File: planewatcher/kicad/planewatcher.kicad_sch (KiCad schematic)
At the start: 7 parts, among them J1 Conn_01x02, J2 RF_IN, J3 FPGA BANK 33, J4 FPGA BANK 35 V1.2/V1.3, J5 BMI-S-209-F

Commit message: work on board layout
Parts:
- renumbered FL3 to FL2, J5 to J3, J3 to J4, J4 to J5
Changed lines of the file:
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@@
 		(dnp no)
 		(fields_autoplaced yes)
-		(property "Reference" "J4"
+		(property "Reference" "J5"
 			(at 105.41 137.16 0)
 			(show_name no)
@@
 			(project "planewatcher"
 				(path "/7a4a4324-e8b8-4d06-b75a-28095d4e9f10"
-					(reference "J4")
+					(reference "J5")
 					(unit 1)
 				)
@@
 		(in_pos_files yes)
 		(dnp no)
-		(property "Reference" "#PWR011"
+		(property "Reference" "#PWR03"
 			(at 146.05 45.72 0)
 			(hide yes)
@@
 			(project "planewatcher"
 				(path "/7a4a4324-e8b8-4d06-b75a-28095d4e9f10"
-					(reference "#PWR011")
+					(reference "#PWR03")
 					(unit 1)
 				)
@@
 		(in_pos_files yes)
 		(dnp no)
-		(property "Reference" "#PWR021"
+		(property "Reference" "#PWR04"
 			(at 185.42 48.26 0)
 			(hide yes)
@@
 			(project "planewatcher"
 				(path "/7a4a4324-e8b8-4d06-b75a-28095d4e9f10"
-					(reference "#PWR021")
+					(reference "#PWR04")
 					(unit 1)
 				)
@@
 		(in_pos_files yes)
 		(dnp no)
-		(property "Reference" "#PWR0146"
+		(property "Reference" "#PWR08"
 			(at 55.88 85.09 0)
 			(hide yes)
@@
 			(project "planewatcher"
 				(path "/7a4a4324-e8b8-4d06-b75a-28095d4e9f10"
-					(reference "#PWR0146")
+					(reference "#PWR08")
 					(unit 1)
 				)
@@
 		(in_pos_files yes)
 		(dnp no)
-		(property "Reference" "#PWR019"
+		(property "Reference" "#PWR013"
 			(at 100.33 111.76 0)
 			(hide yes)
@@
 			(project "planewatcher"
 				(path "/7a4a4324-e8b8-4d06-b75a-28095d4e9f10"
-					(reference "#PWR019")
+					(reference "#PWR013")
 					(unit 1)
 				)
@@
 		(dnp no)
 		(fields_autoplaced yes)
-		(property "Reference" "#PWR078"
+		(property "Reference" "#PWR019"
 			(at 132.08 193.04 0)
 			(hide yes)
@@
 			(project "planewatcher"
 				(path "/7a4a4324-e8b8-4d06-b75a-28095d4e9f10"
-					(reference "#PWR078")
+					(reference "#PWR019")
 					(unit 1)
 				)
@@
 		(in_pos_files yes)
 		(dnp no)
-		(property "Reference" "#PWR04"
+		(property "Reference" "#PWR02"
 			(at 99.06 48.26 0)
 			(hide yes)
@@
 			(project "planewatcher"
 				(path "/7a4a4324-e8b8-4d06-b75a-28095d4e9f10"
-					(reference "#PWR04")
+					(reference "#PWR02")
 					(unit 1)
 				)
@@
 		(in_pos_files yes)
 		(dnp no)
-		(property "Reference" "#PWR039"
+		(property "Reference" "#PWR07"
 			(at 259.08 77.47 0)
 			(hide yes)
@@
 			(project "planewatcher"
 				(path "/7a4a4324-e8b8-4d06-b75a-28095d4e9f10"
-					(reference "#PWR039")
+					(reference "#PWR07")
 					(unit 1)
 				)
@@
 		(dnp no)
 		(fields_autoplaced yes)
-		(property "Reference" "#PWR077"
+		(property "Reference" "#PWR018"
 			(at 78.74 193.04 0)
 			(hide yes)
@@
 			(project "planewatcher"
 				(path "/7a4a4324-e8b8-4d06-b75a-28095d4e9f10"
-					(reference "#PWR077")
+					(reference "#PWR018")
 					(unit 1)
 				)
@@
 		(in_pos_files yes)
 		(dnp no)
-		(property "Reference" "#PWR036"
+		(property "Reference" "#PWR06"
 			(at 236.22 77.47 0)
 			(hide yes)
@@
 			(project "planewatcher"
 				(path "/7a4a4324-e8b8-4d06-b75a-28095d4e9f10"
-					(reference "#PWR036")
+					(reference "#PWR06")
 					(unit 1)
 				)
@@
 		(dnp no)
 		(fields_autoplaced yes)
-		(property "Reference" "J5"
+		(property "Reference" "J3"
 			(at 195.58 106.6799 0)
 			(show_name no)
@@
 			(project "planewatcher"
 				(path "/7a4a4324-e8b8-4d06-b75a-28095d4e9f10"
-					(reference "J5")
+					(reference "J3")
 					(unit 1)
 				)
@@
 		(dnp no)
 		(fields_autoplaced yes)
-		(property "Reference" "J3"
+		(property "Reference" "J4"
 			(at 44.45 137.16 0)
 			(show_name no)
@@
 			(project "planewatcher"
 				(path "/7a4a4324-e8b8-4d06-b75a-28095d4e9f10"
-					(reference "J3")
+					(reference "J4")
 					(unit 1)
 				)
@@
 		(dnp no)
 		(fields_autoplaced yes)
-		(property "Reference" "#PWR037"
+		(property "Reference" "#PWR016"
 			(at 17.78 154.94 0)
 			(hide yes)
@@
 			(project "planewatcher"
 				(path "/7a4a4324-e8b8-4d06-b75a-28095d4e9f10"
-					(reference "#PWR037")
+					(reference "#PWR016")
 					(unit 1)
 				)
@@
 		(dnp no)
 		(fields_autoplaced yes)
-		(property "Reference" "#PWR038"
+		(property "Reference" "#PWR017"
 			(at 71.12 154.94 0)
 			(hide yes)
@@
 			(project "planewatcher"
 				(path "/7a4a4324-e8b8-4d06-b75a-28095d4e9f10"
-					(reference "#PWR038")
+					(reference "#PWR017")
 					(unit 1)
 				)
@@
 		(dnp no)
 		(fields_autoplaced yes)
-		(property "Reference" "#PWR082"
+		(property "Reference" "#PWR015"
 			(at 179.07 124.46 0)
 			(hide yes)
@@
 			(project "planewatcher"
 				(path "/7a4a4324-e8b8-4d06-b75a-28095d4e9f10"
-					(reference "#PWR082")
+					(reference "#PWR015")
 					(unit 1)
 				)
@@
 		(dnp no)
 		(fields_autoplaced yes)
-		(property "Reference" "FL3"
+		(property "Reference" "FL2"
 			(at 149.86 81.28 0)
 			(show_name no)
@@
 			(project "planewatcher"
 				(path "/7a4a4324-e8b8-4d06-b75a-28095d4e9f10"
-					(reference "FL3")
+					(reference "FL2")
 					(unit 1)
 				)
@@
 		(in_pos_files yes)
 		(dnp no)
-		(property "Reference" "#PWR0134"
+		(property "Reference" "#PWR014"
 			(at 153.67 111.76 0)
 			(hide yes)
@@
 			(project "planewatcher"
 				(path "/7a4a4324-e8b8-4d06-b75a-28095d4e9f10"
-					(reference "#PWR0134")
+					(reference "#PWR014")
 					(unit 1)
 				)
@@
 		(dnp no)
 		(fields_autoplaced yes)
-		(property "Reference" "#PWR010"
+		(property "Reference" "#PWR01"
 			(at 34.29 41.91 0)
 			(hide yes)
@@
 			(project "planewatcher"
 				(path "/7a4a4324-e8b8-4d06-b75a-28095d4e9f10"
-					(reference "#PWR010")
+					(reference "#PWR01")
 					(unit 1)
 				)
@@
 		(in_pos_files yes)
 		(dnp no)
-		(property "Reference" "#PWR0145"
+		(property "Reference" "#PWR010"
 			(at 162.56 85.09 0)
 			(hide yes)
@@
 			(project "planewatcher"
 				(path "/7a4a4324-e8b8-4d06-b75a-28095d4e9f10"
-					(reference "#PWR0145")
+					(reference "#PWR010")
 					(unit 1)
 				)
@@
 		(in_pos_files yes)
 		(dnp no)
-		(property "Reference" "#PWR042"
+		(property "Reference" "#PWR05"
 			(at 228.6 48.26 0)
 			(hide yes)
@@
 			(project "planewatcher"
 				(path "/7a4a4324-e8b8-4d06-b75a-28095d4e9f10"
-					(reference "#PWR042")
+					(reference "#PWR05")
 					(unit 1)
 				)
@@
 		(in_pos_files yes)
 		(dnp no)
-		(property "Reference" "#PWR0133"
+		(property "Reference" "#PWR09"
 			(at 109.22 85.09 0)
 			(hide yes)
@@
 			(project "planewatcher"
 				(path "/7a4a4324-e8b8-4d06-b75a-28095d4e9f10"
-					(reference "#PWR0133")
+					(reference "#PWR09")
 					(unit 1)
 				)
@@
 		(in_pos_files yes)
 		(dnp no)
-		(property "Reference" "#PWR015"
+		(property "Reference" "#PWR011"
 			(at 201.93 82.55 0)
 			(hide yes)
@@
 			(project "planewatcher"
 				(path "/7a4a4324-e8b8-4d06-b75a-28095d4e9f10"
-					(reference "#PWR015")
-					(unit 1)
-				)
+					(reference "#PWR011")
+					(unit 1)
+				)

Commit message: finish first rev pcb
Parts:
- J1: footprint (none) -> TerminalBlock_Phoenix:TerminalBlock_Phoenix_MKDS-3-2-5.08_1x02_P5.08mm_Horizontal
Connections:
- net FPGA_3V3: no longer J4.37 (Pin_37), J4.38 (Pin_38), J5.3 (Pin_3), J5.4 (Pin_4)
- no-connect marks 0 -> 8
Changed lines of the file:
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@@
 		(color 0 0 0 0)
 	)
+	(no_connect
+		(at 99.06 189.23)
+	)
+	(no_connect
+		(at 127 189.23)
+	)
+	(no_connect
+		(at 66.04 146.05)
+	)
+	(no_connect
+		(at 83.82 189.23)
+	)
+	(no_connect
+		(at 110.49 189.23)
+	)
+	(no_connect
+		(at 22.86 146.05)
+	)
+	(no_connect
+		(at 50.8 146.05)
+	)
+	(no_connect
+		(at 38.1 146.05)
+	)
 	(wire
 		(pts
@@
 	(wire
 		(pts
-			(xy 50.8 146.05) (xy 66.04 146.05)
-		)
-		(stroke
-			(width 0)
-			(type default)
-		)
-	)
-	(wire
-		(pts
 			(xy 22.86 186.69) (xy 38.1 186.69)
 		)
@@
 	(wire
 		(pts
-			(xy 22.86 146.05) (xy 38.1 146.05)
-		)
-		(stroke
-			(width 0)
-			(type default)
-		)
-	)
-	(wire
-		(pts
 			(xy 254 88.9) (xy 270.51 88.9)
 		)
@@
 	(wire
 		(pts
-			(xy 111.76 189.23) (xy 127 189.23)
-		)
-		(stroke
-			(width 0)
-			(type default)
-		)
-	)
-	(wire
-		(pts
 			(xy 83.82 161.29) (xy 99.06 161.29)
 		)
@@
 	(wire
 		(pts
-			(xy 83.82 189.23) (xy 99.06 189.23)
-		)
-		(stroke
-			(width 0)
-			(type default)
-		)
-	)
-	(wire
-		(pts
 			(xy 254 91.44) (xy 270.51 91.44)
 		)
@@
 			)
 		)
-		(property "Footprint" ""
+		(property "Footprint" "TerminalBlock_Phoenix:TerminalBlock_Phoenix_MKDS-3-2-5.08_1x02_P5.08mm_Horizontal"
 			(at 21.59 33.02 0)
 			(hide yes)
@@
 			)
 		)
-		(property "Value" "FPGA_PWR"
+		(property "Value" "FPGA_VCC"
 			(at 228.6 40.386 0)
 			(show_name no)

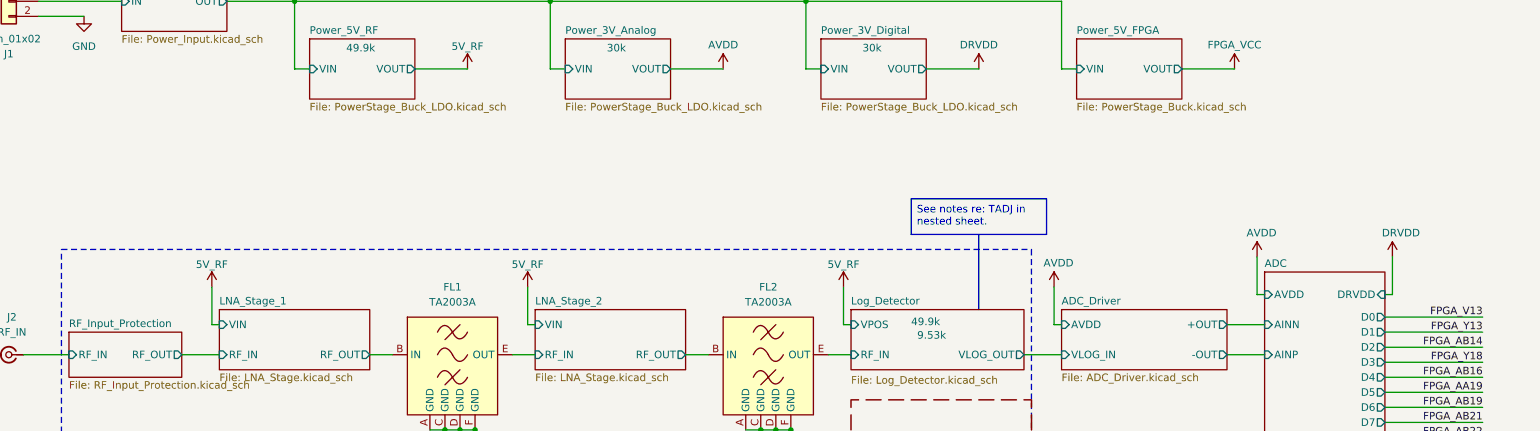
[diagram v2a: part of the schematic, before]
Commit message: add jumpers for testing different power rails & additional test point
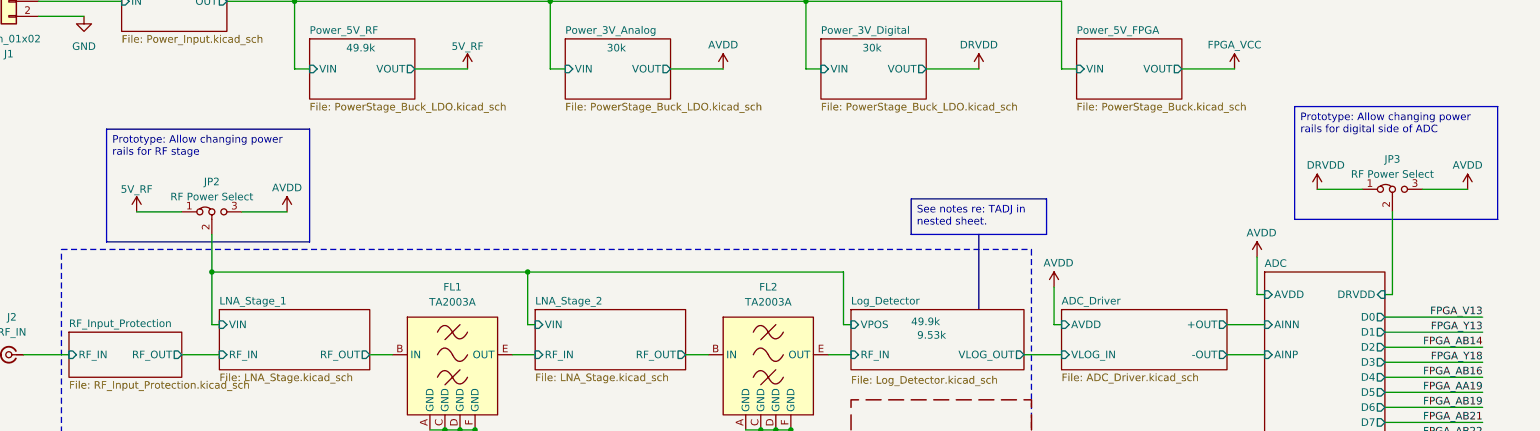
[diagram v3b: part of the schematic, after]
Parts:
- added JP2, JP3: RF Power Select, Connector_PinHeader_2.54mm:PinHeader_1x03_P2.54mm_Vertical, symbol Jumper:Jumper_3_Bridged12
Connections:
- net 5V_RF: now also JP2.1 (A)
- net AVDD: now also JP2.3 (B), JP3.3 (B)
- net DRVDD: now also JP3.1 (A)
- new net ADC/DRVDD: JP3.2 (C)
- new net LNA_Stage_1/VIN: JP2.2 (C)

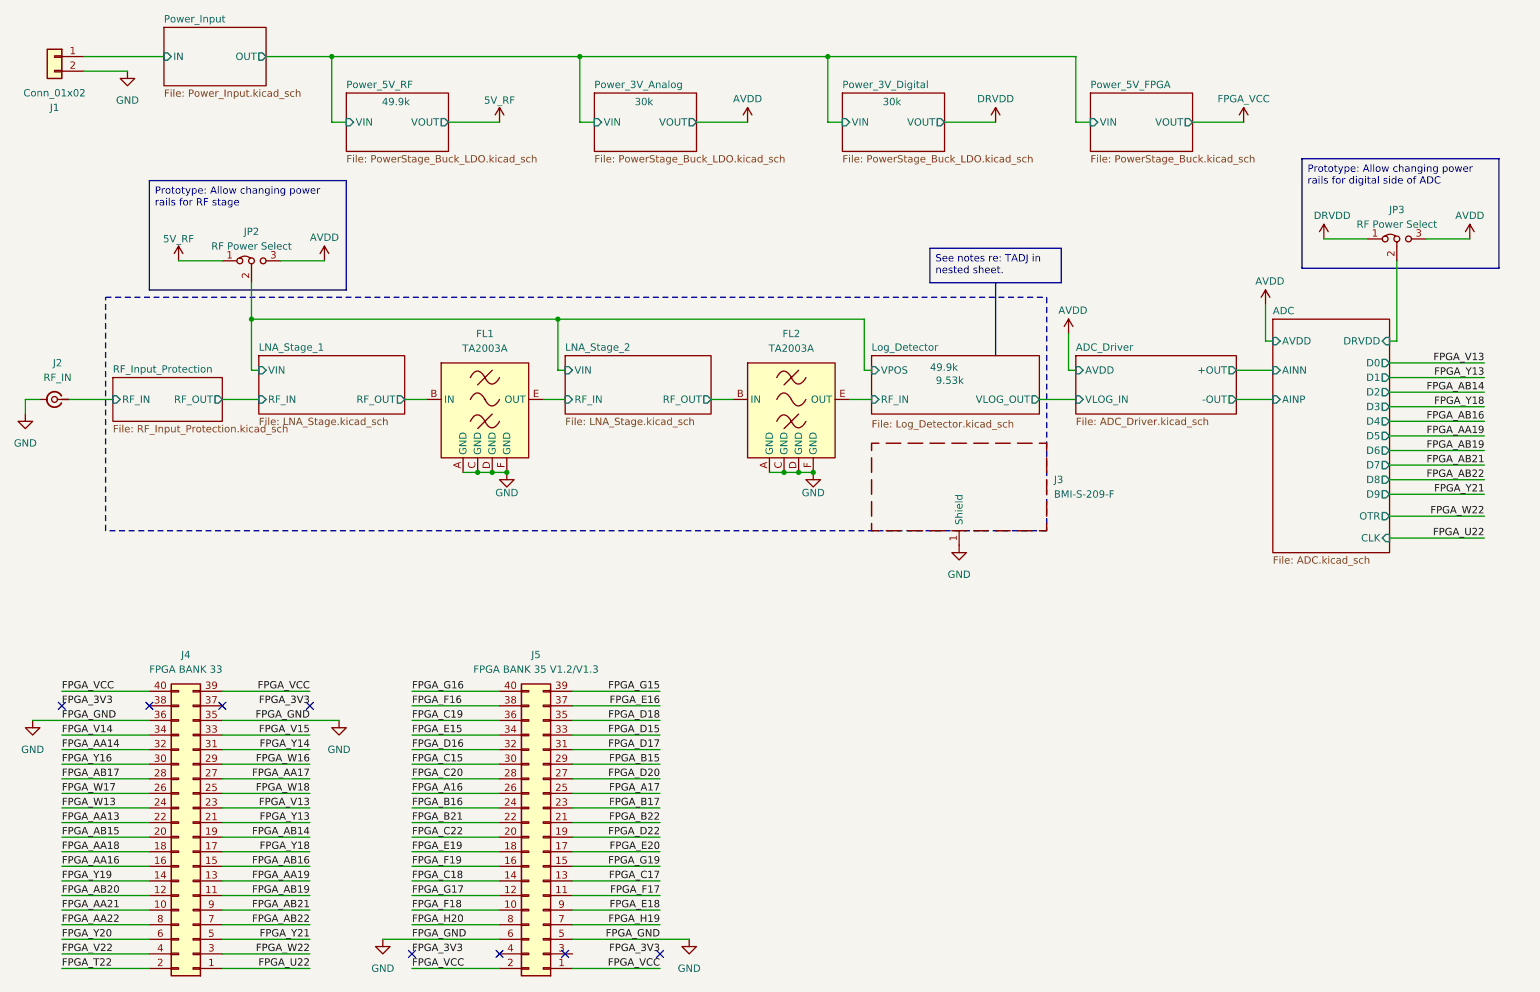
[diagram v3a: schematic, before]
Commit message: address & fix ERC errors/warnings
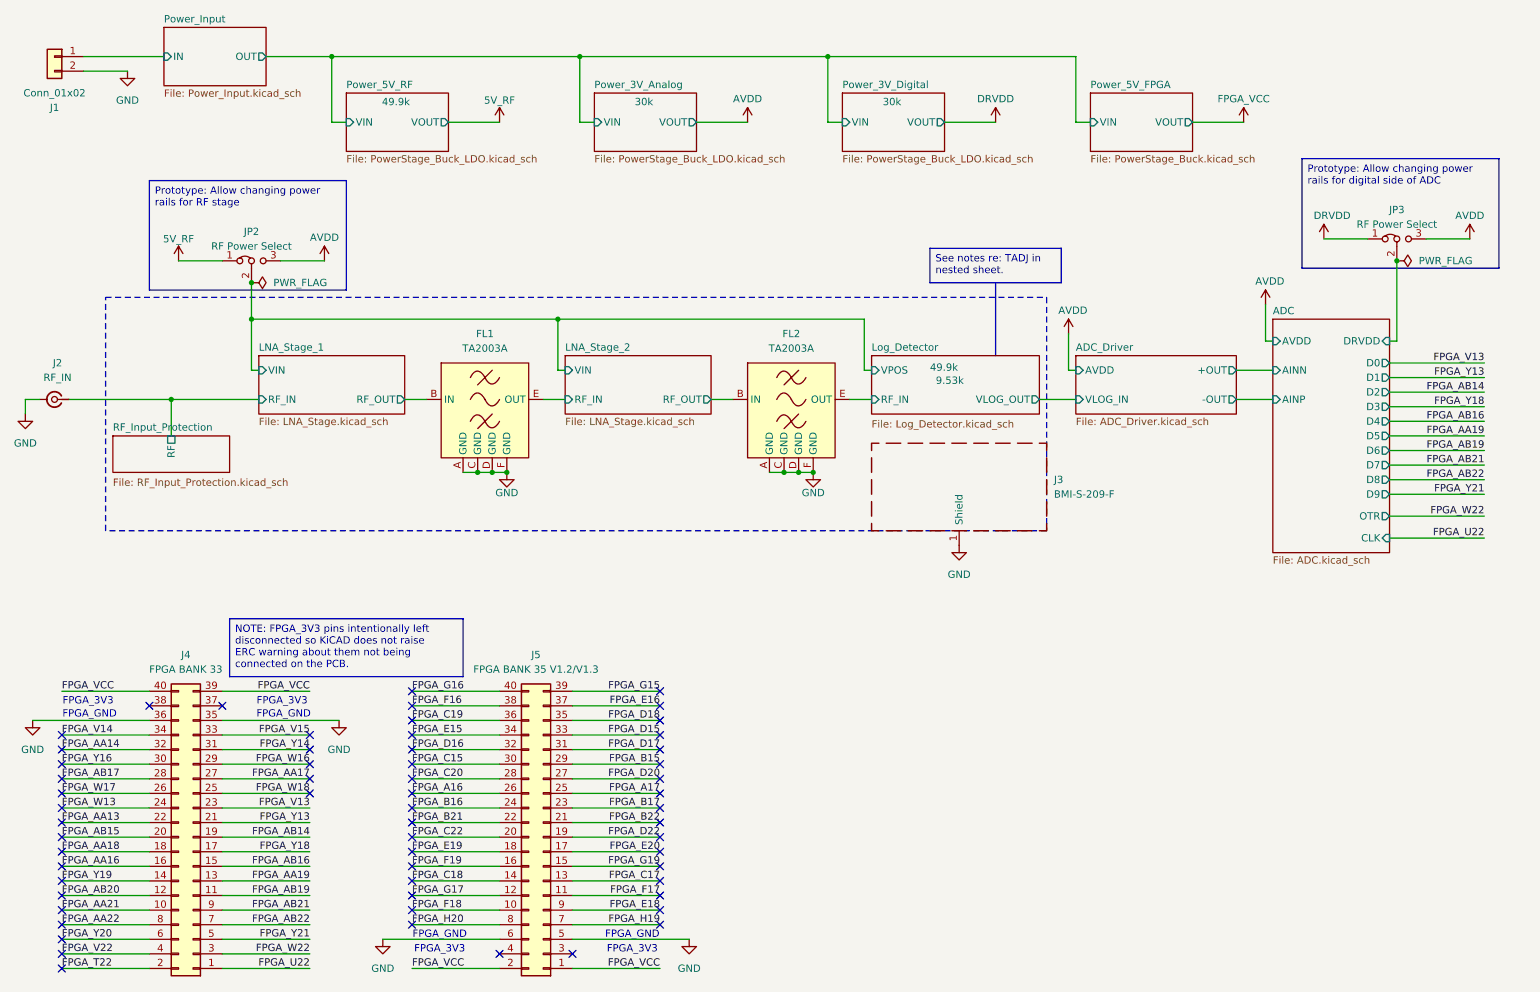
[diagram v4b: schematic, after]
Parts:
- JP2: Notes (none) -> For prototype: Allow changing power rails for RF stage.
- JP3: Notes (none) -> For prototype: Allow changing power rails for digital side 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
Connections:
- net RF_Input_Protection/RF_IN is gone; now on net LNA_Stage_1/RF_IN: J2.1 (In)
- no-connect marks 8 -> 60
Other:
- sheet RF_Input_Protection ports: added RF; removed RF_IN, RF_OUT
- note added: "FPGA_3V3"
- note added: "FPGA_GND"

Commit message: fix all ERC & DRCC errors & warnings
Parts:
- JP3: value RF Power Select -> ADC Digital Power Select
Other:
- sheet ADC ports: added VREF; removed none
- sheet ADC_Driver ports: added ADC_OFFSET; removed none
- sheet Log_Detector ports: added +5V; removed none
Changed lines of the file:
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@@
 	(wire
 		(pts
-			(xy 227.33 92.71) (xy 233.68 92.71)
-		)
-		(stroke
-			(width 0)
-			(type default)
-		)
-	)
-	(wire
-		(pts
 			(xy 156.21 33.02) (xy 199.39 33.02)
 		)
@@
 	(wire
 		(pts
+			(xy 227.33 97.79) (xy 233.68 97.79)
+		)
+		(stroke
+			(width 0)
+			(type default)
+		)
+	)
+	(wire
+		(pts
 			(xy 69.85 33.02) (xy 69.85 44.45)
 		)
@@
 	(wire
 		(pts
+			(xy 227.33 92.71) (xy 233.68 92.71)
+		)
+		(stroke
+			(width 0)
+			(type default)
+		)
+	)
+	(wire
+		(pts
 			(xy 146.05 105.41) (xy 148.59 105.41)
 		)
@@
 	(wire
 		(pts
-			(xy 162.56 78.74) (xy 162.56 87.63)
+			(xy 161.29 78.74) (xy 161.29 90.17)
 		)
 		(stroke
@@
 	(wire
 		(pts
-			(xy 162.56 87.63) (xy 163.83 87.63)
+			(xy 161.29 90.17) (xy 163.83 90.17)
 		)
 		(stroke
@@
 	(wire
 		(pts
-			(xy 162.56 78.74) (xy 109.22 78.74)
+			(xy 161.29 78.74) (xy 109.22 78.74)
 		)
 		(stroke
@@
 	(wire
 		(pts
+			(xy 163.83 87.63) (xy 162.56 87.63)
+		)
+		(stroke
+			(width 0)
+			(type default)
+		)
+	)
+	(wire
+		(pts
 			(xy 43.18 68.58) (xy 50.8 68.58)
 		)
@@
 	(wire
 		(pts
+			(xy 227.33 87.63) (xy 233.68 87.63)
+		)
+		(stroke
+			(width 0)
+			(type default)
+		)
+	)
+	(wire
+		(pts
 			(xy 22.86 151.13) (xy 38.1 151.13)
 		)
@@
 	(wire
 		(pts
+			(xy 162.56 71.12) (xy 162.56 87.63)
+		)
+		(stroke
+			(width 0)
+			(type default)
+		)
+	)
+	(wire
+		(pts
 			(xy 22.86 173.99) (xy 38.1 173.99)
 		)
@@
 	(wire
 		(pts
-			(xy 227.33 87.63) (xy 233.68 87.63)
-		)
-		(stroke
-			(width 0)
-			(type default)
-		)
-	)
-	(wire
-		(pts
 			(xy 83.82 161.29) (xy 99.06 161.29)
 		)
@@
 			)
 		)
-		(property "Value" "RF Power Select"
+		(property "Value" "ADC Digital Power Select"
 			(at 255.27 62.23 0)
 			(show_name no)
@@
 	)
 	(symbol
+		(lib_id "power:+5V")
+		(at 162.56 71.12 0)
+		(unit 1)
+		(body_style 1)
+		(exclude_from_sim no)
+		(in_bom yes)
+		(on_board yes)
+		(in_pos_files yes)
+		(dnp no)
+		(property "Reference" "#PWR0112"
+			(at 162.56 74.93 0)
+			(hide yes)
+			(show_name no)
+			(do_not_autoplace no)
+			(effects
+				(font
+					(size 1.27 1.27)
+				)
+			)
+		)
+		(property "Value" "5V_RF"
+			(at 162.56 67.31 0)
+			(show_name no)
+			(do_not_autoplace no)
+			(effects
+				(font
+					(size 1.27 1.27)
+				)
+			)
+		)
+		(property "Footprint" ""
+			(at 162.56 71.12 0)
+			(hide yes)
+			(show_name no)
+			(do_not_autoplace no)
+			(effects
+				(font
+					(size 1.27 1.27)
+				)
+			)
+		)
+		(property "Datasheet" ""
+			(at 162.56 71.12 0)
+			(hide yes)
+			(show_name no)
+			(do_not_autoplace no)
+			(effects
+				(font
+					(size 1.27 1.27)
+				)
+			)
+		)
+		(property "Description" "Power symbol creates a global label with name \"+5V\""
+			(at 162.56 71.12 0)
+			(hide yes)
+			(show_name no)
+			(do_not_autoplace no)
+			(effects
+				(font
+					(size 1.27 1.27)
+				)
+			)
+		)
+		(pin "1"
+		)
+		(instances
+			(project "planewatcher"
+				(path "/7a4a4324-e8b8-4d06-b75a-28095d4e9f10"
+					(reference "#PWR0112")
+					(unit 1)
+				)
+			)
+		)
+	)
+	(symbol
 		(lib_id "power:GND")
 		(at 71.12 148.59 0)
@@
 		)
 		(pin "VPOS" input
-			(at 163.83 87.63 180)
+			(at 163.83 90.17 180)
 			(effects
 				(font
@@
 			)
 		)
+		(pin "+5V" input
+			(at 163.83 87.63 180)
+			(effects
+				(font
+					(size 1.27 1.27)
+				)
+				(justify left)
+			)
+		)
 		(instances
 			(project "planewatcher"
@@
 	(sheet
 		(at 199.39 85.09)
-		(size 27.94 10.16)
+		(size 27.94 15.24)
 		(exclude_from_sim no)
 		(in_bom yes)
@@
 		)
 		(property "Sheetfile" "ADC_Driver.kicad_sch"
-			(at 199.39 95.8346 0)
+			(at 199.39 100.9146 0)
 			(show_name no)
 			(do_not_autoplace no)
@@
 			)
 		)
+		(pin "ADC_OFFSET" input
+			(at 227.33 97.79 0)
+			(effects
+				(font
+					(size 1.27 1.27)
+				)
+				(justify right)
+			)
+		)
 		(instances
 			(project "planewatcher"
@@
 		)
 		(pin "AINN" input
-			(at 233.68 87.63 180)
+			(at 233.68 92.71 180)
 			(effects
 				(font
@@
 		)
 		(pin "AINP" input
-			(at 233.68 92.71 180)
+			(at 233.68 87.63 180)
 			(effects
 				(font
@@
 			)
 		)
+		(pin "VREF" output
+			(at 233.68 97.79 180)
+			(effects
+				(font
+					(size 1.27 1.27)
+				)
+				(justify left)
+			)
+		)
